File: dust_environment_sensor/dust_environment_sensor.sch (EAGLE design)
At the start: 1 part, among them U1 LTP5901

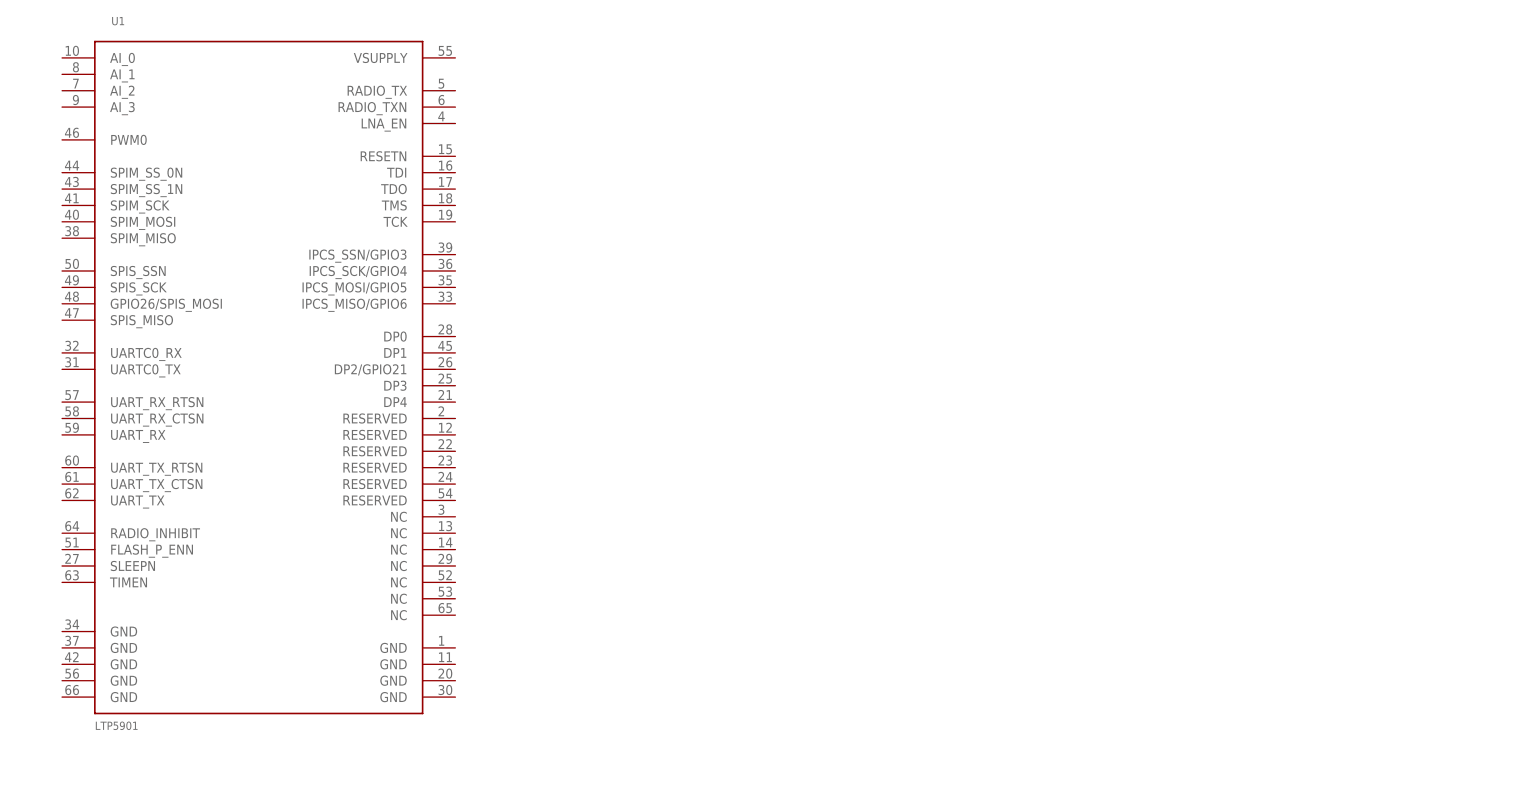
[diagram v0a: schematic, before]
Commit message: Putting together dust sensor mote
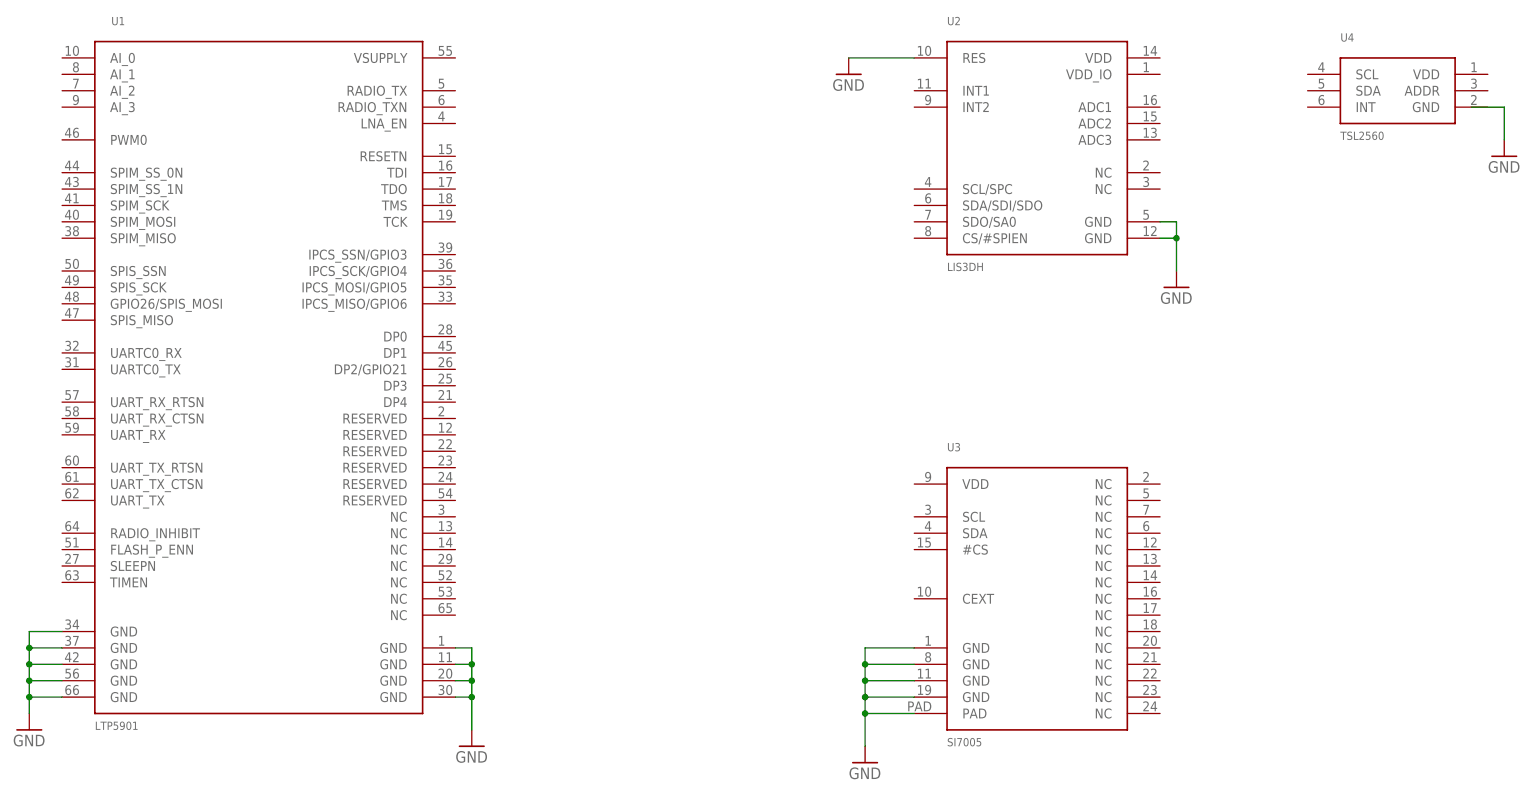
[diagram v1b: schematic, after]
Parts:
- added U2: LIS3DH, Cool_Electricity:LIS3DH
- added U3: SI7005, Cool_Electricity:SI7005
- added U4: TSL2560, Cool_Electricity:TSL2560
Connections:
- new net GND: U1.GND@1, U1.GND@2, U1.GND@3, U1.GND@4, U1.GND@5, U1.GND@6, U1.GND@7, U1.GND@8, U1.GND@9, U2.GND@1, U2.GND@2, U2.RES, U3.GND@1, U3.GND@2, U3.GND@3, U3.GND@4, U3.PAD
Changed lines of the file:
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@@
 <parts>
 <part name="U1" library="Cool_Electricity" deviceset="LTP5901" device=""/>
+<part name="U2" library="Cool_Electricity" deviceset="LIS3DH" device=""/>
+<part name="U3" library="Cool_Electricity" deviceset="SI7005" device=""/>
+<part name="U4" library="Cool_Electricity" deviceset="TSL2560" device=""/>
+<part name="GND1" library="supply1" deviceset="GND" device=""/>
+<part name="GND2" library="supply1" deviceset="GND" device=""/>
+<part name="GND3" library="supply1" deviceset="GND" device=""/>
+<part name="GND4" library="supply1" deviceset="GND" device=""/>
+<part name="GND5" library="supply1" deviceset="GND" device=""/>
+<part name="GND6" library="supply1" deviceset="GND" device=""/>
 </parts>
 <sheets>
@@
 <instances>
 <instance part="U1" gate="G$1" x="71.12" y="63.5"/>
+<instance part="U2" gate="G$1" x="190.5" y="99.06"/>
+<instance part="U3" gate="G$1" x="190.5" y="22.86"/>
+<instance part="U4" gate="G$1" x="246.38" y="104.14"/>
+<instance part="GND1" gate="1" x="210.82" y="73.66"/>
+<instance part="GND2" gate="1" x="261.62" y="93.98"/>
+<instance part="GND3" gate="1" x="162.56" y="0"/>
+<instance part="GND4" gate="1" x="101.6" y="2.54"/>
+<instance part="GND5" gate="1" x="33.02" y="5.08"/>
+<instance part="GND6" gate="1" x="160.02" y="106.68"/>
 </instances>
 <busses>
 </busses>
 <nets>
+<net name="GND" class="0">
+<segment>
+<pinref part="U1" gate="G$1" pin="GND@1"/>
+<pinref part="GND4" gate="1" pin="GND"/>
+<wire x1="99.06" y1="17.78" x2="101.6" y2="17.78" width="0.1524" layer="91"/>
+<wire x1="101.6" y1="17.78" x2="101.6" y2="15.24" width="0.1524" layer="91"/>
+<pinref part="U1" gate="G$1" pin="GND@2"/>
+<wire x1="101.6" y1="15.24" x2="101.6" y2="12.7" width="0.1524" layer="91"/>
+<wire x1="101.6" y1="12.7" x2="101.6" y2="10.16" width="0.1524" layer="91"/>
+<wire x1="101.6" y1="10.16" x2="101.6" y2="5.08" width="0.1524" layer="91"/>
+<wire x1="99.06" y1="15.24" x2="101.6" y2="15.24" width="0.1524" layer="91"/>
+<junction x="101.6" y="15.24"/>
+<pinref part="U1" gate="G$1" pin="GND@3"/>
+<wire x1="99.06" y1="12.7" x2="101.6" y2="12.7" width="0.1524" layer="91"/>
+<junction x="101.6" y="12.7"/>
+<pinref part="U1" gate="G$1" pin="GND@4"/>
+<wire x1="99.06" y1="10.16" x2="101.6" y2="10.16" width="0.1524" layer="91"/>
+<junction x="101.6" y="10.16"/>
+</segment>
+<segment>
+<pinref part="U1" gate="G$1" pin="GND@5"/>
+<pinref part="GND5" gate="1" pin="GND"/>
+<wire x1="38.1" y1="20.32" x2="33.02" y2="20.32" width="0.1524" layer="91"/>
+<wire x1="33.02" y1="20.32" x2="33.02" y2="17.78" width="0.1524" layer="91"/>
+<pinref part="U1" gate="G$1" pin="GND@6"/>
+<wire x1="33.02" y1="17.78" x2="33.02" y2="15.24" width="0.1524" layer="91"/>
+<wire x1="33.02" y1="15.24" x2="33.02" y2="12.7" width="0.1524" layer="91"/>
+<wire x1="33.02" y1="12.7" x2="33.02" y2="10.16" width="0.1524" layer="91"/>
+<wire x1="33.02" y1="10.16" x2="33.02" y2="7.62" width="0.1524" layer="91"/>
+<wire x1="38.1" y1="17.78" x2="33.02" y2="17.78" width="0.1524" layer="91"/>
+<junction x="33.02" y="17.78"/>
+<pinref part="U1" gate="G$1" pin="GND@7"/>
+<wire x1="38.1" y1="15.24" x2="33.02" y2="15.24" width="0.1524" layer="91"/>
+<junction x="33.02" y="15.24"/>
+<pinref part="U1" gate="G$1" pin="GND@8"/>
+<wire x1="38.1" y1="12.7" x2="33.02" y2="12.7" width="0.1524" layer="91"/>
+<junction x="33.02" y="12.7"/>
+<pinref part="U1" gate="G$1" pin="GND@9"/>
+<wire x1="38.1" y1="10.16" x2="33.02" y2="10.16" width="0.1524" layer="91"/>
+<junction x="33.02" y="10.16"/>
+</segment>
+<segment>
+<pinref part="U3" gate="G$1" pin="GND@1"/>
+<pinref part="GND3" gate="1" pin="GND"/>
+<wire x1="170.18" y1="17.78" x2="162.56" y2="17.78" width="0.1524" layer="91"/>
+<wire x1="162.56" y1="17.78" x2="162.56" y2="15.24" width="0.1524" layer="91"/>
+<pinref part="U3" gate="G$1" pin="PAD"/>
+<wire x1="162.56" y1="15.24" x2="162.56" y2="12.7" width="0.1524" layer="91"/>
+<wire x1="162.56" y1="12.7" x2="162.56" y2="10.16" width="0.1524" layer="91"/>
+<wire x1="162.56" y1="10.16" x2="162.56" y2="7.62" width="0.1524" layer="91"/>
+<wire x1="162.56" y1="7.62" x2="162.56" y2="2.54" width="0.1524" layer="91"/>
+<wire x1="170.18" y1="7.62" x2="162.56" y2="7.62" width="0.1524" layer="91"/>
+<junction x="162.56" y="7.62"/>
+<pinref part="U3" gate="G$1" pin="GND@4"/>
+<wire x1="170.18" y1="10.16" x2="162.56" y2="10.16" width="0.1524" layer="91"/>
+<junction x="162.56" y="10.16"/>
+<pinref part="U3" gate="G$1" pin="GND@3"/>
+<wire x1="170.18" y1="12.7" x2="162.56" y2="12.7" width="0.1524" layer="91"/>
+<junction x="162.56" y="12.7"/>
+<pinref part="U3" gate="G$1" pin="GND@2"/>
+<wire x1="170.18" y1="15.24" x2="162.56" y2="15.24" width="0.1524" layer="91"/>
+<junction x="162.56" y="15.24"/>
+</segment>
+<segment>
+<pinref part="U2" gate="G$1" pin="GND@1"/>
+<pinref part="GND1" gate="1" pin="GND"/>
+<wire x1="208.28" y1="83.82" x2="210.82" y2="83.82" width="0.1524" layer="91"/>
+<wire x1="210.82" y1="83.82" x2="210.82" y2="81.28" width="0.1524" layer="91"/>
+<pinref part="U2" gate="G$1" pin="GND@2"/>
+<wire x1="210.82" y1="81.28" x2="210.82" y2="76.2" width="0.1524" layer="91"/>
+<wire x1="208.28" y1="81.28" x2="210.82" y2="81.28" width="0.1524" layer="91"/>
+<junction x="210.82" y="81.28"/>
+</segment>
+<segment>
+<pinref part="U2" gate="G$1" pin="RES"/>
+<pinref part="GND6" gate="1" pin="GND"/>
+<wire x1="170.18" y1="109.22" x2="160.02" y2="109.22" width="0.1524" layer="91"/>
+</segment>
+<segment>
+<pinref part="GND2" gate="1" pin="GND"/>
+<wire x1="256.54" y1="101.6" x2="261.62" y2="101.6" width="0.1524" layer="91"/>
+<wire x1="261.62" y1="101.6" x2="261.62" y2="96.52" width="0.1524" layer="91"/>
+</segment>
+</net>
 </nets>
 </sheet>

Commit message: Battery holder
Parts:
- added J1: (no value), Cool_Electricity:BX0036
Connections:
- net GND: now also J1.NEG
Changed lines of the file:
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@@
 <part name="GND5" library="supply1" deviceset="GND" device=""/>
 <part name="GND6" library="supply1" deviceset="GND" device=""/>
+<part name="J1" library="Cool_Electricity" deviceset="BX0036" device=""/>
+<part name="GND7" library="supply1" deviceset="GND" device=""/>
 </parts>
 <sheets>
@@
 <instance part="GND5" gate="1" x="33.02" y="5.08"/>
 <instance part="GND6" gate="1" x="160.02" y="106.68"/>
+<instance part="J1" gate="G$1" x="259.08" y="38.1"/>
+<instance part="GND7" gate="1" x="256.54" y="27.94"/>
 </instances>
 <busses>
@@
 <wire x1="261.62" y1="101.6" x2="261.62" y2="96.52" width="0.1524" layer="91"/>
 </segment>
+<segment>
+<pinref part="GND7" gate="1" pin="GND"/>
+<pinref part="J1" gate="G$1" pin="NEG"/>
+<wire x1="256.54" y1="30.48" x2="259.08" y2="30.48" width="0.1524" layer="91"/>
+<wire x1="259.08" y1="30.48" x2="259.08" y2="35.56" width="0.1524" layer="91"/>
+</segment>
 </net>

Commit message: more work on dust sensor
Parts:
- added C1, C3, C5: 100n, rcl:C-USC0603
- added C2: 10u, rcl:C-USC0603
- added C31, C32: 22p, SparkFun:CAP0603
- added C33, C34, C41: .1u, SparkFun:CAP0603
- added C4: 100u, rcl:C-USC0603
- added C6: (no value), rcl:C-USC0603
- added C7: 4.7u, rcl:C-USC0603
- added JP1: (no value), custom:FTDI_CABLESIP
- added JP2: AVR_SPI_PRG_6NS, SparkFun:AVR_SPI_PRG_6NS
- added R1, R2: 2.2k, resistor:R-US_R0603
- added R46: 10k, SparkFun:RESISTOR0603
- added U5: ATMEGA168, SparkFun:ATMEGA168
- added X1: 32.768KHz, WSNlib:XTALABS07
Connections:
- new net 5V: C33.2, C34.2, JP1.VCC, JP2.2, R46.2, U5.AVCC, U5.VCC@1, U5.VCC@2
- new net ACCEL_INT1: U2.INT1
- new net ACCEL_INT2: U2.INT2
- new net ATMEGA_TO_MOTE: JP1.RXD, U1.UART_RX, U5.PD1(TXD)
- new net HUMID_#CS: U3.#CS
- new net I2C_SCL: R1.1, U2.SCL/SPC, U3.SCL, U4.SCL, U5.PC5(ADC5/SCL)
- new net I2C_SDA: R2.1, U2.SDA/SDI/SDO, U3.SDA, U4.SDA, U5.PC4(ADC4/SDA)
- new net LIGHT_INT: U4.INT
- new net MISO: JP2.1, U5.PB4(MISO)
- new net MOSI: JP2.4, U5.PB3(MOSI/OC2)
- new net MOTE_TO_ATMEGA: JP1.TXD, U1.UART_TX, U5.PD0(RXD)
- new net N$1: C7.1, U3.CEXT
- new net N$2: C31.1, U5.PB6(XTAL1/TOSC1), X1.B
- new net N$4: C32.1, U5.PB7(XTAL2/TOSC2), X1.A
- new net RST: C41.1, JP2.5, R46.1, U5.PC6(/RESET)
- new net RTS#: C41.2, JP1.RTS
- new net SCLK: JP2.3, U5.PB5(SCK)
- new net VCC: C1.1, C2.1, C3.1, C4.1, C5.1, C6.1, J1.POS, R1.2, R2.2, U1.VSUPPLY, U2.CS/#SPIEN, U2.SDO/SA0, U2.VDD, U3.VDD, U4.VDD
- net GND: now also C1.2, C2.2, C3.2, C31.2, C32.2, C33.1, C34.1, C4.2, C5.2, C6.2, C7.2, JP1.CTS, JP1.GND, JP2.6, U4.GND, U5.AGND, U5.GND@1, U5.GND@2
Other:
- note added: "AN0"
- note added: "AN1"
- note added: "AN2"
- note added: "AN3"
- note added: "AN4"
- note added: "AN5"
- note added: "DIG0"
- note added: "DIG1"
- note added: "DIG10 (PWM)"
- note added: "DIG11 (PWM)"
- note added: "DIG12"
- note added: "DIG13"
- note added: "DIG14"
- note added: "DIG15"
- note added: "DIG16"
- note added: "DIG17"
- note added: "DIG18"
- note added: "DIG19"
- note added: "DIG2"
- note added: "DIG3"
- note added: "DIG4"
- note added: "DIG5 (PWM)"
- note added: "DIG6 (PWM)"
- note added: "DIG7"
- note added: "DIG8"
- note added: "DIG9 (PWM)"
- note added: "I2C ADDRESS: 00110010"
- moved on the sheet: U4

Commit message: BOM done
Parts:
- added JP3: .1" header, con-lstb:MA06-2
- added LED1: RED, led:LEDCHIPLED_0805
- added R3: 15, resistor:R-US_R0603
- added R4: 120, SparkFun:RESISTOR0603
- added STANDOFF1, STANDOFF2, STANDOFF3, STANDOFF4: STAND-OFF, SparkFun-Electromechanical:STAND-OFF
- C4: device rcl:C-USC0603 -> SparkFun-Capacitors:CAP_POL1206-KIT
- C6: value (none) -> 100n
- J1: value (none) -> 3.6V Lithium C cell
- JP1: value (none) -> 87758-1016; device custom:FTDI_CABLESIP -> con-molex:87758-1016
- U5: value ATMEGA168 -> ATMEGA328P
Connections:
- removed net 5V: C33.2, C34.2, JP1.VCC, JP2.2, R46.2, U5.AVCC, U5.VCC@1, U5.VCC@2
- removed net ATMEGA_TO_MOTE: JP1.RXD, U1.UART_RX, U5.PD1(TXD)
- removed net HUMID_#CS: U3.#CS
- removed net MOTE_TO_ATMEGA: JP1.TXD, U1.UART_TX, U5.PD0(RXD)
- new net ATMEGA_RX: JP3.7, U5.PD0(RXD)
- new net ATMEGA_TX: JP3.9, U5.PD1(TXD)
- new net FLASH_P_ENN: JP1-2.S, U1.FLASH_P_ENN
- new net HUMID_VCC: R3.2, U5.PC2(ADC2)
- new net IPCS_MISO: JP1-5.S, U1.IPCS_MISO/GPIO6
- new net IPCS_MOSI: JP1-4.S, U1.IPCS_MOSI/GPIO5
- new net IPCS_SCK: JP1-3.S, U1.IPCS_SCK/GPIO4
- new net IPCS_SSN: JP1-1.S, U1.IPCS_SSN/GPIO3
- new net LED1: R4.2, U5.PC3(ADC3)
- new net MOTE_API_RX: JP3.10, U1.UART_RX
- new net MOTE_API_TX: JP3.8, U1.UART_TX
- new net MOTE_CLI_RX: JP1-10.S, U1.UARTC0_RX
- new net MOTE_CLI_TX: JP1-9.S, U1.UARTC0_TX
- new net MOTE_RADIO_INHIBIT: U1.RADIO_INHIBIT, U5.PB0(ICP)
- new net MOTE_RESETN: JP1-6.S, U1.RESETN, U5.PD7(AIN1)
- new net MOTE_RX_CTSN: U1.UART_RX_CTSN, U5.PD6(AIN0)
- new net MOTE_RX_RTSN: U1.UART_RX_RTSN, U5.PD5(T1)
- new net MOTE_SLEEPN: U1.SLEEPN, U5.PB1(OC1A)
- new net MOTE_TIMEN: U1.TIMEN, U5.PB2(SS/OC1B)
- new net MOTE_TX_CTSN: U1.UART_TX_CTSN, U5.PD4(XCK/T0)
- new net MOTE_TX_RTSN: U1.UART_TX_RTSN, U5.PD3(INT1)
- new net N$3: C5.1, R3.1, U3.VDD
- new net N$5: LED1.A, R4.1
- new net VBATT: C4.+, J1.POS, JP3.4
- net ACCEL_INT1: now also U5.PD2(INT0)
- net ACCEL_INT2: now also U5.PC0(ADC0)
- net GND: now also C4.-, JP1-8.S, JP3.1, JP3.3, LED1.C, U3.#CS, U5.ADC6, U5.ADC7; no longer C4.2, JP1.CTS, JP1.GND
- net LIGHT_INT: now also U5.PC1(ADC1)
- net RTS#: now also JP3.11; no longer JP1.RTS
- net VCC: now also C33.2, C34.2, JP1-7.S, JP2.2, JP3.6, R46.2, U5.AVCC, U5.VCC@1, U5.VCC@2; no longer C4.1, C5.1, J1.POS, U3.VDD
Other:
- note added: "I2C ADDRESS: 10000000"
- note added: "MOUNTING HOLES"

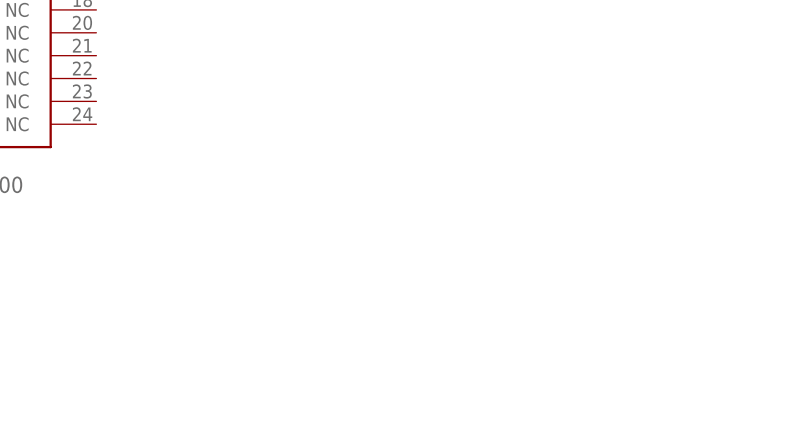
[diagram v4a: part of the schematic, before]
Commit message: Added new version of power strip
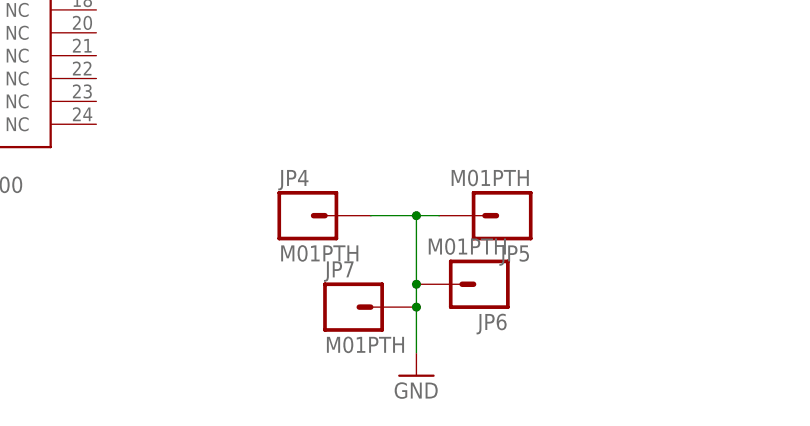
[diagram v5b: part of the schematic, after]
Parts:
- added JP4, JP5, JP6, JP7: M01PTH, SparkFun-Connectors:M01PTH
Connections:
- net GND: now also JP4.1, JP5.1, JP6.1, JP7.1
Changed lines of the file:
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@@
 <part name="R4" library="SparkFun" deviceset="RESISTOR" device="0603" value="120"/>
 <part name="GND15" library="SparkFun" deviceset="GND" device=""/>
+<part name="JP4" library="SparkFun-Connectors" deviceset="M01" device="PTH"/>
+<part name="GND16" library="supply1" deviceset="GND" device=""/>
+<part name="JP5" library="SparkFun-Connectors" deviceset="M01" device="PTH"/>
+<part name="JP6" library="SparkFun-Connectors" deviceset="M01" device="PTH"/>
+<part name="JP7" library="SparkFun-Connectors" deviceset="M01" device="PTH"/>
 </parts>
 <sheets>
@@
 <instance part="R4" gate="G$1" x="520.7" y="78.74" rot="R90"/>
 <instance part="GND15" gate="1" x="520.7" y="60.96"/>
+<instance part="JP4" gate="G$1" x="231.14" y="-2.54"/>
+<instance part="GND16" gate="1" x="243.84" y="-20.32"/>
+<instance part="JP5" gate="G$1" x="254" y="-2.54" rot="R180"/>
+<instance part="JP6" gate="G$1" x="251.46" y="-10.16" rot="R180"/>
+<instance part="JP7" gate="G$1" x="236.22" y="-12.7"/>
 </instances>
 <busses>
@@
 <wire x1="520.7" y1="63.5" x2="520.7" y2="66.04" width="0.1524" layer="91"/>
 </segment>
+<segment>
+<pinref part="JP4" gate="G$1" pin="1"/>
+<pinref part="JP5" gate="G$1" pin="1"/>
+<wire x1="238.76" y1="-2.54" x2="243.84" y2="-2.54" width="0.1524" layer="91"/>
+<pinref part="GND16" gate="1" pin="GND"/>
+<wire x1="243.84" y1="-2.54" x2="246.38" y2="-2.54" width="0.1524" layer="91"/>
+<wire x1="243.84" y1="-2.54" x2="243.84" y2="-10.16" width="0.1524" layer="91"/>
+<junction x="243.84" y="-2.54"/>
+<pinref part="JP6" gate="G$1" pin="1"/>
+<wire x1="243.84" y1="-10.16" x2="243.84" y2="-12.7" width="0.1524" layer="91"/>
+<junction x="243.84" y="-10.16"/>
+<pinref part="JP7" gate="G$1" pin="1"/>
+<wire x1="243.84" y1="-12.7" x2="243.84" y2="-17.78" width="0.1524" layer="91"/>
+<junction x="243.84" y="-12.7"/>
+</segment>
 </net>
